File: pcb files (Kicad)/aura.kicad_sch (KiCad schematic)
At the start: 85 parts, among them J1 nice!view, SW1 SW_Push, SW10 SW_Push, SW11 SW_Push, SW12 SW_Push, SW13 SW_Push, SW14 SW_Push, SW15 SW_Push, SW16 SW_Push, SW17 SW_Push, SW18 SW_Push, SW19 SW_Push, SW2 SW_Push, SW20 SW_Push, SW21 SW_Push, SW22 SW_Push, SW23 SW_Push, SW24 SW_Push, SW25 SW_Push, SW26 SW_Push, SW27 SW_Push, SW28 SW_Push, SW29 SW_Push, SW3 SW_Push, SW30 SW_Push, SW31 SW_Push, SW32 SW_Push, SW33 SW_Push, SW34 SW_Push, SW35 SW_Push, SW36 SW_Push, SW37 Reset Switch, SW4 SW_Push, SW5 SW_Push, SW6 SW_Push, SW7 SW_Push, SW8 SW_Push, SW9 SW_Push, U1 Seeeduino Xiao nRF52840 Plus

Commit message: potentially done, still need to cleanup
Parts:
- removed BAT1: Battery, Connector_JST:JST_ACH_BM02B-ACHSS-GAN-ETF_1x02-1MP_P1.20mm_Vertical polarity independent, symbol Device:Battery
- removed PWR1: Power Switch, PCM_marbastlib-various:SW_MSK12C02-HB, symbol Switch:SW_SPDT
- added SW38: Soft Off, Button_Switch_SMD:Panasonic_EVQPUL_EVQPUC, symbol Switch:SW_Push
- SW37: footprint PCM_marbastlib-various:SW_SPST_SKQG_WithStem -> Button_Switch_SMD:Panasonic_EVQPUL_EVQPUC
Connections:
- net GND: now also SW38.1
- net soft off: now reaches U1.7 (P1.11)
- net soft off: now also SW38.2
- no-connect marks 8 -> 6
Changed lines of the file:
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@@
 	)
 	(no_connect
-		(at 237.49 121.92)
-	)
-	(no_connect
 		(at 259.08 86.36)
 	)
@@
 	)
 	(no_connect
-		(at 119.38 129.54)
-	)
-	(no_connect
 		(at 237.49 114.3)
 	)
@@
 	(wire
 		(pts
-			(xy 133.35 121.92) (xy 119.38 121.92)
-		)
-		(stroke
-			(width 0)
-			(type default)
-		)
-	)
-	(wire
-		(pts
 			(xy 217.17 58.42) (xy 237.49 58.42)
 		)
@@
 	(wire
 		(pts
-			(xy 119.38 121.92) (xy 119.38 124.46)
-		)
-		(stroke
-			(width 0)
-			(type default)
-		)
-	)
-	(wire
-		(pts
 			(xy 146.05 86.36) (xy 146.05 68.58)
 		)
@@
 		)
 	)
+	(global_label "soft off"
+		(shape input)
+		(at 199.39 142.24 0)
+		(effects
+			(font
+				(size 1.27 1.27)
+			)
+			(justify left)
+		)
+		(property "Intersheetrefs" "${INTERSHEET_REFS}"
+			(at 199.39 142.24 0)
+			(effects
+				(font
+					(size 1.27 1.27)
+				)
+				(hide yes)
+			)
+		)
+	)
 	(global_label "col2"
 		(shape input)
@@
 		)
 	)
+	(global_label "soft off"
+		(shape input)
+		(at 237.49 121.92 180)
+		(effects
+			(font
+				(size 1.27 1.27)
+			)
+			(justify right)
+		)
+		(property "Intersheetrefs" "${INTERSHEET_REFS}"
+			(at 237.49 121.92 0)
+			(effects
+				(font
+					(size 1.27 1.27)
+				)
+				(hide yes)
+			)
+		)
+	)
 	(global_label "col1"
 		(shape input)
@@
 		)
 	)
-	(global_label "BAT-"
-		(shape input)
-		(at 133.35 132.08 270)
-		(effects
-			(font
-				(size 1.27 1.27)
-			)
-			(justify right)
-		)
-		(property "Intersheetrefs" "${INTERSHEET_REFS}"
-			(at 133.35 132.08 0)
-			(effects
-				(font
-					(size 1.27 1.27)
-				)
-				(hide yes)
-			)
-		)
-	)
 	(global_label "col4"
 		(shape input)
@@
 		)
 	)
-	(global_label "BAT+"
-		(shape input)
-		(at 109.22 127 180)
-		(effects
-			(font
-				(size 1.27 1.27)
-			)
-			(justify right)
-		)
-		(property "Intersheetrefs" "${INTERSHEET_REFS}"
-			(at 109.22 127 0)
-			(effects
-				(font
-					(size 1.27 1.27)
-				)
-				(hide yes)
-			)
-		)
-	)
 	(symbol
 		(lib_id "chocV-rescue:GND-power")
@@
 			)
 		)
-		(property "Footprint" "PCM_marbastlib-various:SW_SPST_SKQG_WithStem"
+		(property "Footprint" "Button_Switch_SMD:Panasonic_EVQPUL_EVQPUC"
 			(at 194.31 121.92 0)
 			(effects
@@
 	)
 	(symbol
-		(lib_id "Switch:SW_SPDT")
-		(at 114.3 127 0)
+		(lib_id "chocV-rescue:GND-power")
+		(at 189.23 142.24 0)
 		(unit 1)
 		(exclude_from_sim no)
@@
 		(on_board yes)
 		(dnp no)
-		(fields_autoplaced yes)
-		(property "Reference" "PWR1"
-			(at 114.3 118.11 0)
+		(property "Reference" "#PWR02"
+			(at 189.23 148.59 0)
 			(effects
 				(font
 					(size 1.27 1.27)
 				)
+				(hide yes)
 			)
 		)
-		(property "Value" "Power Switch"
-			(at 114.3 120.65 0)
+		(property "Value" "GND"
+			(at 189.357 146.6342 0)
 			(effects
 				(font
@@
 			)
 		)
-		(property "Footprint" "PCM_marbastlib-various:SW_MSK12C02-HB"
-			(at 114.3 127 0)
+		(property "Footprint" ""
+			(at 189.23 142.24 0)
 			(effects
 				(font
@@
 			)
 		)
-		(property "Datasheet" "~"
-			(at 114.3 127 0)
+		(property "Datasheet" ""
+			(at 189.23 142.24 0)
 			(effects
 				(font
@@
 		)
 		(property "Description" ""
-			(at 114.3 127 0)
+			(at 189.23 142.24 0)
 			(effects
 				(font
@@
 		(pin "1"
 		)
-		(pin "2"
-		)
-		(pin "3"
-		)
 		(instances
-			(project "chocV-hotswap-solder-xiao"
+			(project "aura"
 				(path "/4fa2c0fe-ec5a-40ab-b5c3-47c4f0712337"
-					(reference "PWR1")
+					(reference "#PWR02")
 					(unit 1)
 				)
@@
 	)
 	(symbol
-		(lib_id "Device:Battery")
-		(at 133.35 127 0)
+		(lib_id "Switch:SW_Push")
+		(at 194.31 142.24 0)
 		(unit 1)
 		(exclude_from_sim no)
@@
 		(on_board yes)
 		(dnp no)
-		(fields_autoplaced yes)
-		(property "Reference" "BAT1"
-			(at 137.16 125.3489 0)
+		(property "Reference" "SW38"
+			(at 194.31 135.001 0)
 			(effects
 				(font
 					(size 1.27 1.27)
 				)
-				(justify left)
 			)
 		)
-		(property "Value" "Battery"
-			(at 137.16 127.8889 0)
+		(property "Value" "Soft Off"
+			(at 194.31 137.3124 0)
 			(effects
 				(font
 					(size 1.27 1.27)
 				)
-				(justify left)
 			)
 		)
-		(property "Footprint" "Connector_JST:JST_ACH_BM02B-ACHSS-GAN-ETF_1x02-1MP_P1.20mm_Vertical polarity independent"
-			(at 133.35 125.476 90)
+		(property "Footprint" "Button_Switch_SMD:Panasonic_EVQPUL_EVQPUC"
+			(at 194.31 137.16 0)
 			(effects
 				(font
@@
 		)
 		(property "Datasheet" "~"
-			(at 133.35 125.476 90)
+			(at 194.31 137.16 0)
 			(effects
 				(font
@@
 		)
 		(property "Description" ""
-			(at 133.35 127 0)
+			(at 194.31 142.24 0)
 			(effects
 				(font
@@
 		)
 		(instances
-			(project "chocV-hotswap-solder-xiao"
+			(project "aura"
 				(path "/4fa2c0fe-ec5a-40ab-b5c3-47c4f0712337"
-					(reference "BAT1")
+					(reference "SW38")
 					(unit 1)
 				)

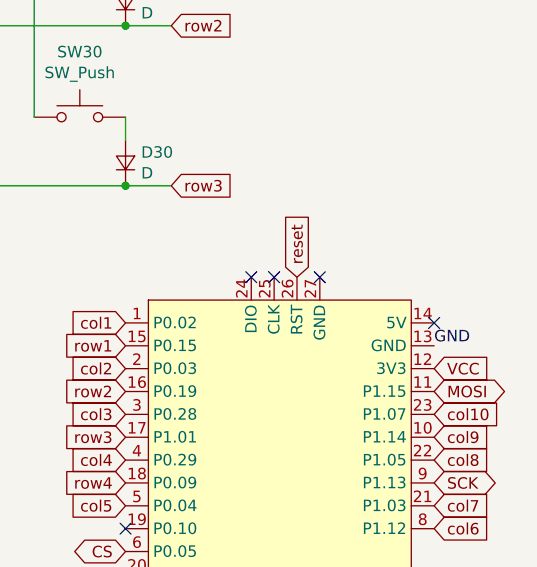
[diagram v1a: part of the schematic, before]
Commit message: moved stuff, added images of proto
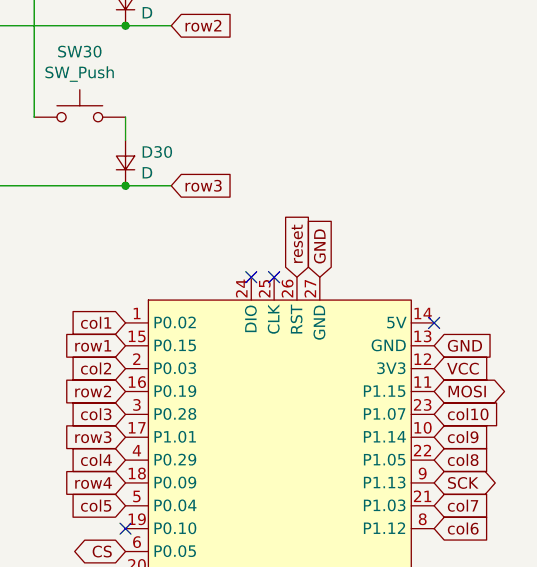
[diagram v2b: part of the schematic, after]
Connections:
- net GND: now also U1.27 (GND)
- no-connect marks 6 -> 5
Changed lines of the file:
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@@
-	)
-	(no_connect
-		(at 259.08 86.36)
 	)
 	(no_connect
@@
 			(width 0)
 			(type default)
-		)
-	)
-	(label "GND"
-		(at 271.78 93.98 0)
-		(effects
-			(font
-				(size 1.27 1.27)
-			)
-			(justify left bottom)
 		)
 	)
@@
 		)
 	)
+	(global_label "GND"
+		(shape input)
+		(at 271.78 93.98 0)
+		(fields_autoplaced yes)
+		(effects
+			(font
+				(size 1.27 1.27)
+			)
+			(justify left)
+		)
+		(property "Intersheetrefs" "${INTERSHEET_REFS}"
+			(at 277.9815 93.98 0)
+			(effects
+				(font
+					(size 1.27 1.27)
+				)
+				(justify left)
+				(hide yes)
+			)
+		)
+	)
 	(global_label "col4"
 		(shape input)
@@
 				(hide yes)
 			)
+		)
+	)
+	(global_label "GND"
+		(shape input)
+		(at 259.08 86.36 90)
+		(fields_autoplaced yes)
+		(effects
+			(font
+				(size 1.27 1.27)
+			)
+			(justify left)
+		)
+		(property "Intersheetrefs" "${INTERSHEET_REFS}"
+			(at 259.08 80.1585 90)
+			(effects
+				(font
+					(size 1.27 1.27)
+				)
+				(justify left)
+				(hide yes)
+			)
